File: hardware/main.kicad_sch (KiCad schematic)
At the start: 15 parts, among them J10 AS0BC21-S30BM-7H, J4 98424-G52-04ALF, J5 Bus_PCI_Express_Mini

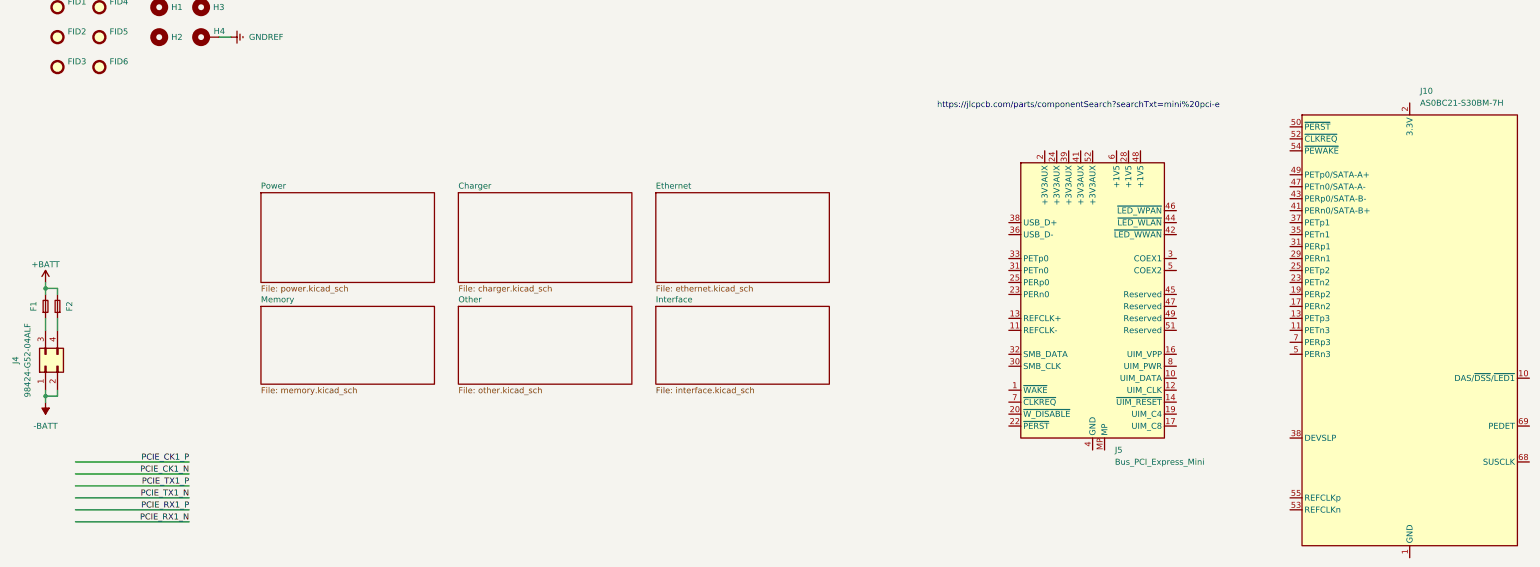
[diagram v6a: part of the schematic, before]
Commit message: pinlayout for pci-e
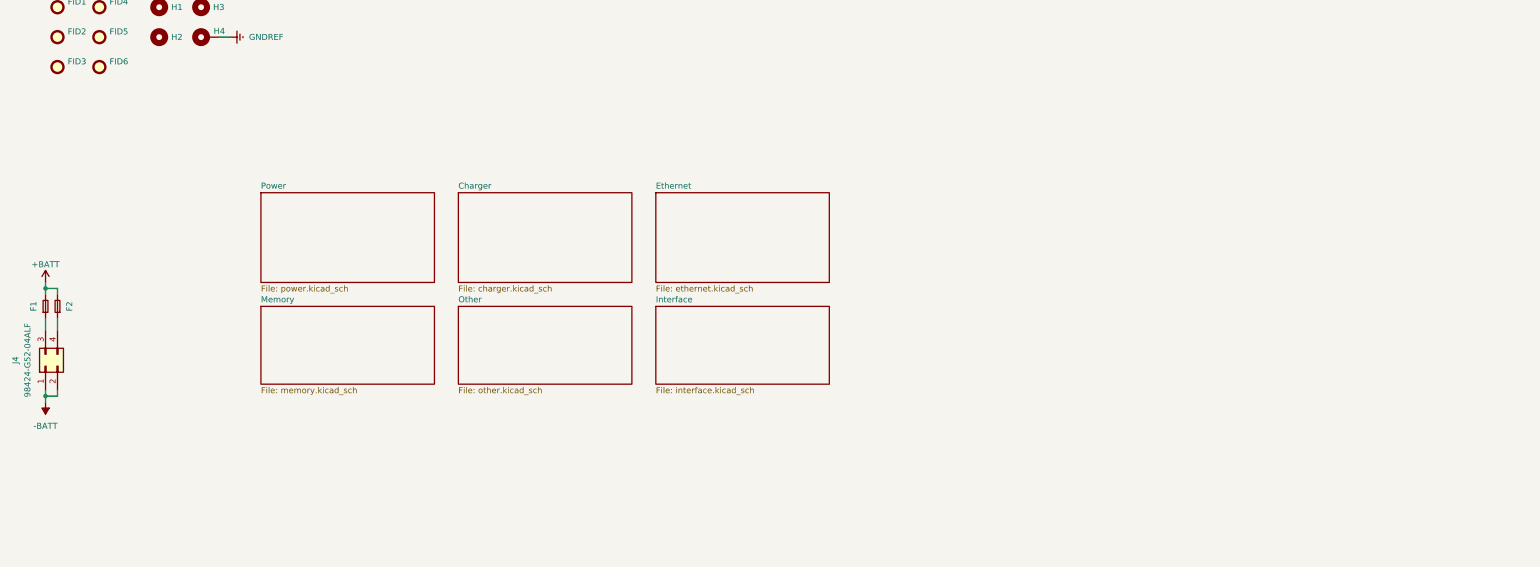
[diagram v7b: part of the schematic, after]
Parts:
- removed J10: AS0BC21-S30BM-7H, MAS_Package_std:Bus_M.2_Socket_M, symbol Connector:Bus_M.2_Socket_M
- removed J5: Bus_PCI_Express_Mini, MAS_Package_std:BUS_PCI_Express_Mini_Dual, symbol Connector:Bus_PCI_Express_Mini
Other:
- note removed: "https://jlcpcb.com/parts/componentSearch?searchTxt=mini%20pci-e"
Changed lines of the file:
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@@
-    (stroke (width 0) (type default))
-  )
-  (wire (pts (xy 36.83 130.81) (xy 60.96 130.81))
     (stroke (width 0) (type default))
   )
@@
     (stroke (width 0) (type default))
   )
-  (wire (pts (xy 36.83 143.51) (xy 60.96 143.51))
-    (stroke (width 0) (type default))
-  )
-  (wire (pts (xy 36.83 133.35) (xy 60.96 133.35))
-    (stroke (width 0) (type default))
-  )
   (wire (pts (xy 30.48 116.84) (xy 30.48 118.11))
     (stroke (width 0) (type default))
@@
     (stroke (width 0) (type default))
   )
-  (wire (pts (xy 36.83 135.89) (xy 60.96 135.89))
-    (stroke (width 0) (type default))
-  )
   (wire (pts (xy 33.02 93.98) (xy 33.02 95.25))
     (stroke (width 0) (type default))
@@
   (wire (pts (xy 30.48 100.33) (xy 30.48 102.87))
     (stroke (width 0) (type default))
-  )
-  (wire (pts (xy 36.83 138.43) (xy 60.96 138.43))
-    (stroke (width 0) (type default))
-  )
-  (wire (pts (xy 36.83 140.97) (xy 60.96 140.97))
-    (stroke (width 0) (type default))
-  )
-  (text "https://jlcpcb.com/parts/componentSearch?searchTxt=mini%20pci-e"
-    (at 219.71 55.88 0)
-    (effects (font (size 1.27 1.27)) (justify left bottom))
-  )
-  (label "PCIE_CK1_P" (at 60.96 130.81 180) (fields_autoplaced)
-    (effects (font (size 1.27 1.27)) (justify right bottom))
-  )
-  (label "PCIE_TX1_N" (at 60.96 138.43 180) (fields_autoplaced)
-    (effects (font (size 1.27 1.27)) (justify right bottom))
-  )
-  (label "PCIE_RX1_N" (at 60.96 143.51 180) (fields_autoplaced)
-    (effects (font (size 1.27 1.27)) (justify right bottom))
-  )
-  (label "PCIE_TX1_P" (at 60.96 135.89 180) (fields_autoplaced)
-    (effects (font (size 1.27 1.27)) (justify right bottom))
-  )
-  (label "PCIE_RX1_P" (at 60.96 140.97 180) (fields_autoplaced)
-    (effects (font (size 1.27 1.27)) (justify right bottom))
-  )
-  (label "PCIE_CK1_N" (at 60.96 133.35 180) (fields_autoplaced)
-    (effects (font (size 1.27 1.27)) (justify right bottom))
   )
   (symbol (lib_id "Mechanical:MountingHole_Pad") (at 64.77 40.64 90) (unit 1)
@@
     )
   )
-  (symbol (lib_id "Connector:Bus_M.2_Socket_M") (at 320.04 102.87 0) (unit 1)
-    (in_bom yes) (on_board yes) (dnp no) (fields_autoplaced)
-    (property "Reference" "J10" (at 322.2341 52.07 0)
-      (effects (font (size 1.27 1.27)) (justify left))
-    )
-    (property "Value" "AS0BC21-S30BM-7H" (at 322.2341 54.61 0)
-      (effects (font (size 1.27 1.27)) (justify left))
-    )
-    (property "Footprint" "MAS_Package_std:Bus_M.2_Socket_M" (at 320.04 76.2 0)
-      (effects (font (size 1.27 1.27)) hide)
-    )
-    (property "Datasheet" "http://read.pudn.com/downloads794/doc/project/3133918/PCIe_M.2_Electromechanical_Spec_Rev1.0_Final_11012013_RS_Clean.pdf#page=155" (at 320.04 76.2 0)
-      (effects (font (size 1.27 1.27)) hide)
-    )
-    (property "lcsc" "C2832351" (at 320.04 102.87 0)
-      (effects (font (size 1.27 1.27)) hide)
-    )
-    (pin "1")
-    (pin "10")
-    (pin "11")
-    (pin "12")
-    (pin "13")
-    (pin "14")
-    (pin "15")
-    (pin "16")
-    (pin "17")
-    (pin "18")
-    (pin "19")
-    (pin "2")
-    (pin "20")
-    (pin "21")
-    (pin "22")
-    (pin "23")
-    (pin "24")
-    (pin "25")
-    (pin "26")
-    (pin "27")
-    (pin "28")
-    (pin "29")
-    (pin "3")
-    (pin "30")
-    (pin "31")
-    (pin "32")
-    (pin "33")
-    (pin "34")
-    (pin "35")
-    (pin "36")
-    (pin "37")
-    (pin "38")
-    (pin "39")
-    (pin "4")
-    (pin "40")
-    (pin "41")
-    (pin "42")
-    (pin "43")
-    (pin "44")
-    (pin "45")
-    (pin "46")
-    (pin "47")
-    (pin "48")
-    (pin "49")
-    (pin "5")
-    (pin "50")
-    (pin "51")
-    (pin "52")
-    (pin "53")
-    (pin "54")
-    (pin "55")
-    (pin "56")
-    (pin "57")
-    (pin "58")
-    (pin "6")
-    (pin "67")
-    (pin "68")
-    (pin "69")
-    (pin "7")
-    (pin "70")
-    (pin "71")
-    (pin "72")
-    (pin "73")
-    (pin "74")
-    (pin "75")
-    (pin "8")
-    (pin "9")
-    (instances
-      (project "main"
-        (path "/c6e5d5ba-43a3-4ff8-a766-3efdb024d1f4"
-          (reference "J10") (unit 1)
-        )
-      )
-    )
-  )
   (symbol (lib_id "Mechanical:Fiducial") (at 33.02 34.29 0) (unit 1)
     (in_bom no) (on_board yes) (dnp no)
@@
         )
       )
-    )
-  )
-  (symbol (lib_id "Connector:Bus_PCI_Express_Mini") (at 252.73 97.79 0) (unit 1)
-    (in_bom yes) (on_board yes) (dnp no) (fields_autoplaced)
-    (property "Reference" "J5" (at 257.4641 128.27 0)
-      (effects (font (size 1.27 1.27)) (justify left))
-    )
-    (property "Value" "Bus_PCI_Express_Mini" (at 257.4641 130.81 0)
-      (effects (font (size 1.27 1.27)) (justify left))
-    )
-    (property "Footprint" "MAS_Package_std:BUS_PCI_Express_Mini_Dual" (at 252.73 97.79 0)
-      (effects (font (size 1.27 1.27)) hide)
-    )
-    (property "Datasheet" "~" (at 248.92 127 0)
-      (effects (font (size 1.27 1.27)) hide)
-    )
-    (pin "1")
-    (pin "10")
-    (pin "11")
-    (pin "12")
-    (pin "13")
-    (pin "14")
-    (pin "15")
-    (pin "16")
-    (pin "17")
-    (pin "18")
-    (pin "19")
-    (pin "2")
-    (pin "20")
-    (pin "21")
-    (pin "22")
-    (pin "23")
-    (pin "24")
-    (pin "25")
-    (pin "26")
-    (pin "27")
-    (pin "28")
-    (pin "29")
-    (pin "3")
-    (pin "30")
-    (pin "31")
-    (pin "32")
-    (pin "33")
-    (pin "34")
-    (pin "35")
-    (pin "36")
-    (pin "37")
-    (pin "38")
-    (pin "39")
-    (pin "4")
-    (pin "40")
-    (pin "41")
-    (pin "42")
-    (pin "43")
-    (pin "44")
-    (pin "45")
-    (pin "46")
-    (pin "47")
-    (pin "48")
-    (pin "49")
-    (pin "5")
-    (pin "50")
-    (pin "51")
-    (pin "52")
-    (pin "6")
-    (pin "7")
-    (pin "8")
-    (pin "9")
-    (pin "MP")
-    (instances
-      (project "main"
-        (path "/c6e5d5ba-43a3-4ff8-a766-3efdb024d1f4"
-          (reference "J5") (unit 1)
-        )
-      )

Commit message: update pcb
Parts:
- removed H4: H, MountingHole:MountingHole_3.2mm_M3_DIN965_Pad, symbol Mechanical:MountingHole_Pad
- added H4: H, MountingHole:MountingHole_3.2mm_M3_DIN965_Pad, symbol Mechanical:MountingHole
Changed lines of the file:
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@@
-    (stroke (width 0) (type default))
-  )
-  (wire (pts (xy 69.85 40.64) (xy 67.31 40.64))
     (stroke (width 0) (type default))
   )
@@
   (wire (pts (xy 30.48 100.33) (xy 30.48 102.87))
     (stroke (width 0) (type default))
-  )
-  (symbol (lib_id "Mechanical:MountingHole_Pad") (at 64.77 40.64 90) (unit 1)
-    (in_bom no) (on_board yes) (dnp no)
-    (property "Reference" "H4" (at 68.58 39.37 90)
-      (effects (font (size 1.27 1.27)) (justify left))
-    )
-    (property "Value" "H" (at 65.913 38.1 0)
-      (effects (font (size 1.27 1.27)) (justify left) hide)
-    )
-    (property "Footprint" "MountingHole:MountingHole_3.2mm_M3_DIN965_Pad" (at 64.77 40.64 0)
-      (effects (font (size 1.27 1.27)) hide)
-    )
-    (property "Datasheet" "~" (at 64.77 40.64 0)
-      (effects (font (size 1.27 1.27)) hide)
-    )
-    (property "chipdip" "" (at 64.77 40.64 0)
-      (effects (font (size 1.27 1.27)) hide)
-    )
-    (pin "1")
-    (instances
-      (project "main"
-        (path "/c6e5d5ba-43a3-4ff8-a766-3efdb024d1f4"
-          (reference "H4") (unit 1)
-        )
-      )
-    )
-  )
-  (symbol (lib_id "power:GNDREF") (at 69.85 40.64 90) (unit 1)
-    (in_bom yes) (on_board yes) (dnp no) (fields_autoplaced)
-    (property "Reference" "#PWR0110" (at 76.2 40.64 0)
-      (effects (font (size 1.27 1.27)) hide)
-    )
-    (property "Value" "GNDREF" (at 73.66 40.6399 90)
-      (effects (font (size 1.27 1.27)) (justify right))
-    )
-    (property "Footprint" "" (at 69.85 40.64 0)
-      (effects (font (size 1.27 1.27)) hide)
-    )
-    (property "Datasheet" "" (at 69.85 40.64 0)
-      (effects (font (size 1.27 1.27)) hide)
-    )
-    (pin "1")
-    (instances
-      (project "main"
-        (path "/c6e5d5ba-43a3-4ff8-a766-3efdb024d1f4"
-          (reference "#PWR0110") (unit 1)
-        )
-      )
-    )
   )
   (symbol (lib_id "Mechanical:Fiducial") (at 41.91 46.99 0) (unit 1)
@@
         )
       )
+    )
+  )
+  (symbol (lib_id "Mechanical:MountingHole") (at 63.5 40.64 0) (unit 1)
+    (in_bom no) (on_board yes) (dnp no)
+    (property "Reference" "H4" (at 66.04 40.64 0)
+      (effects (font (size 1.27 1.27)) (justify left))
+    )
+    (property "Value" "H" (at 66.04 41.783 0)
+      (effects (font (size 1.27 1.27)) (justify left) hide)
+    )
+    (property "Footprint" "MountingHole:MountingHole_3.2mm_M3_DIN965_Pad" (at 63.5 40.64 0)
+      (effects (font (size 1.27 1.27)) hide)
+    )
+    (property "Datasheet" "~" (at 63.5 40.64 0)
+      (effects (font (size 1.27 1.27)) hide)
+    )
+    (property "chipdip" "" (at 63.5 40.64 0)
+      (effects (font (size 1.27 1.27)) hide)
+    )
+    (instances
+      (project "main"
+        (path "/c6e5d5ba-43a3-4ff8-a766-3efdb024d1f4"
+          (reference "H4") (unit 1)
+        )
+      )
